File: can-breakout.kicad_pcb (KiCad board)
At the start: 2 copper layers, 87 x 59.9 mm, 53 parts, among them J201 Screw_Terminal_01x02, J301 SEAM-50-02.0-S-08-2-A-K-TR-ND, J302 SEAF-50-05.0-S-08-2-A-K-TR, J401 Screw_Terminal_01x02, U101 UA78M05IDCYR, U102 MIC5365-3.3YD5-TR, U201 SN65HVD256, U401 SN65HVD256

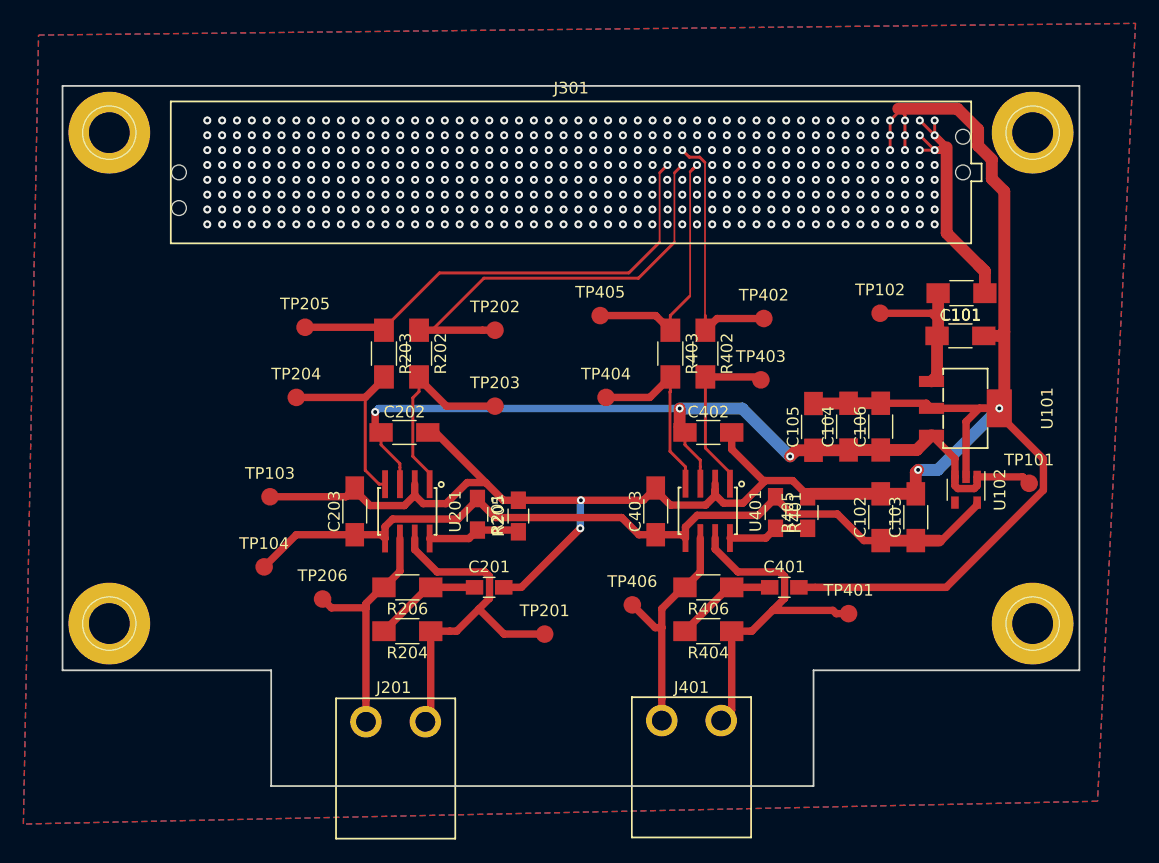
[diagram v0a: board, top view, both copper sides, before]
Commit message: Add silkscreen markings
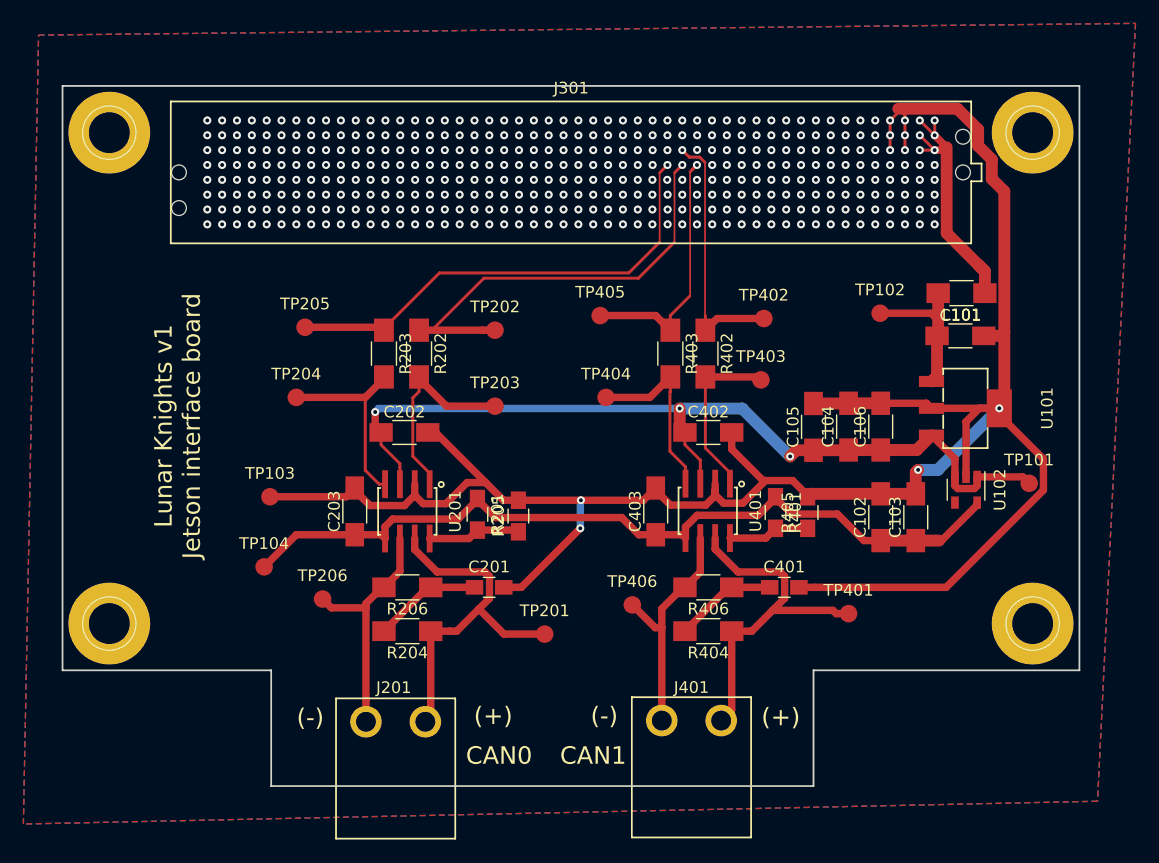
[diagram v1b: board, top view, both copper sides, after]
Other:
- board text added: "(+)"
- board text added: "(-)"
- board text added: "CAN0"
- board text added: "CAN1"
- board text added: "Lunar Knights v1 Jetson interface board"
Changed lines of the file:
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@@
     (area 53.15 87.25 148.300001 157.227401)
     (thickness 1.6)
-    (drawings 9)
+    (drawings 16)
     (tracks 685)
     (zones 0)
@@
     )
   )
+  (gr_text "Lunar Knights v1\nJetson interface board\n" (at 66.35 121.7 90) (layer F.SilkS)
+    (effects (font (size 1.5 1.5) (thickness 0.3)))
+  )
+  (gr_text "(-)" (at 77.7 146.65) (layer F.SilkS)
+    (effects (font (size 1.5 1.5) (thickness 0.3)))
+  )
+  (gr_text "(+)" (at 93.35 146.5) (layer F.SilkS)
+    (effects (font (size 1.5 1.5) (thickness 0.3)))
+  )
+  (gr_text CAN1 (at 101.9 149.9) (layer F.SilkS)
+    (effects (font (size 1.5 1.5) (thickness 0.3)))
+  )
+  (gr_text CAN0 (at 93.85 149.9) (layer F.SilkS)
+    (effects (font (size 1.5 1.5) (thickness 0.3)))
+  )
+  (gr_text "(-)" (at 102.85 146.5) (layer F.SilkS)
+    (effects (font (size 1.5 1.5) (thickness 0.3)))
+  )
+  (gr_text "(+)\n" (at 117.95 146.6) (layer F.SilkS)
+    (effects (font (size 1.5 1.5) (thickness 0.3)))
+  )
   (gr_line (start 74.35 142.6) (end 56.5 142.6) (layer Edge.Cuts) (width 0.15))
